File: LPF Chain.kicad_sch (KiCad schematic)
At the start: 24 parts

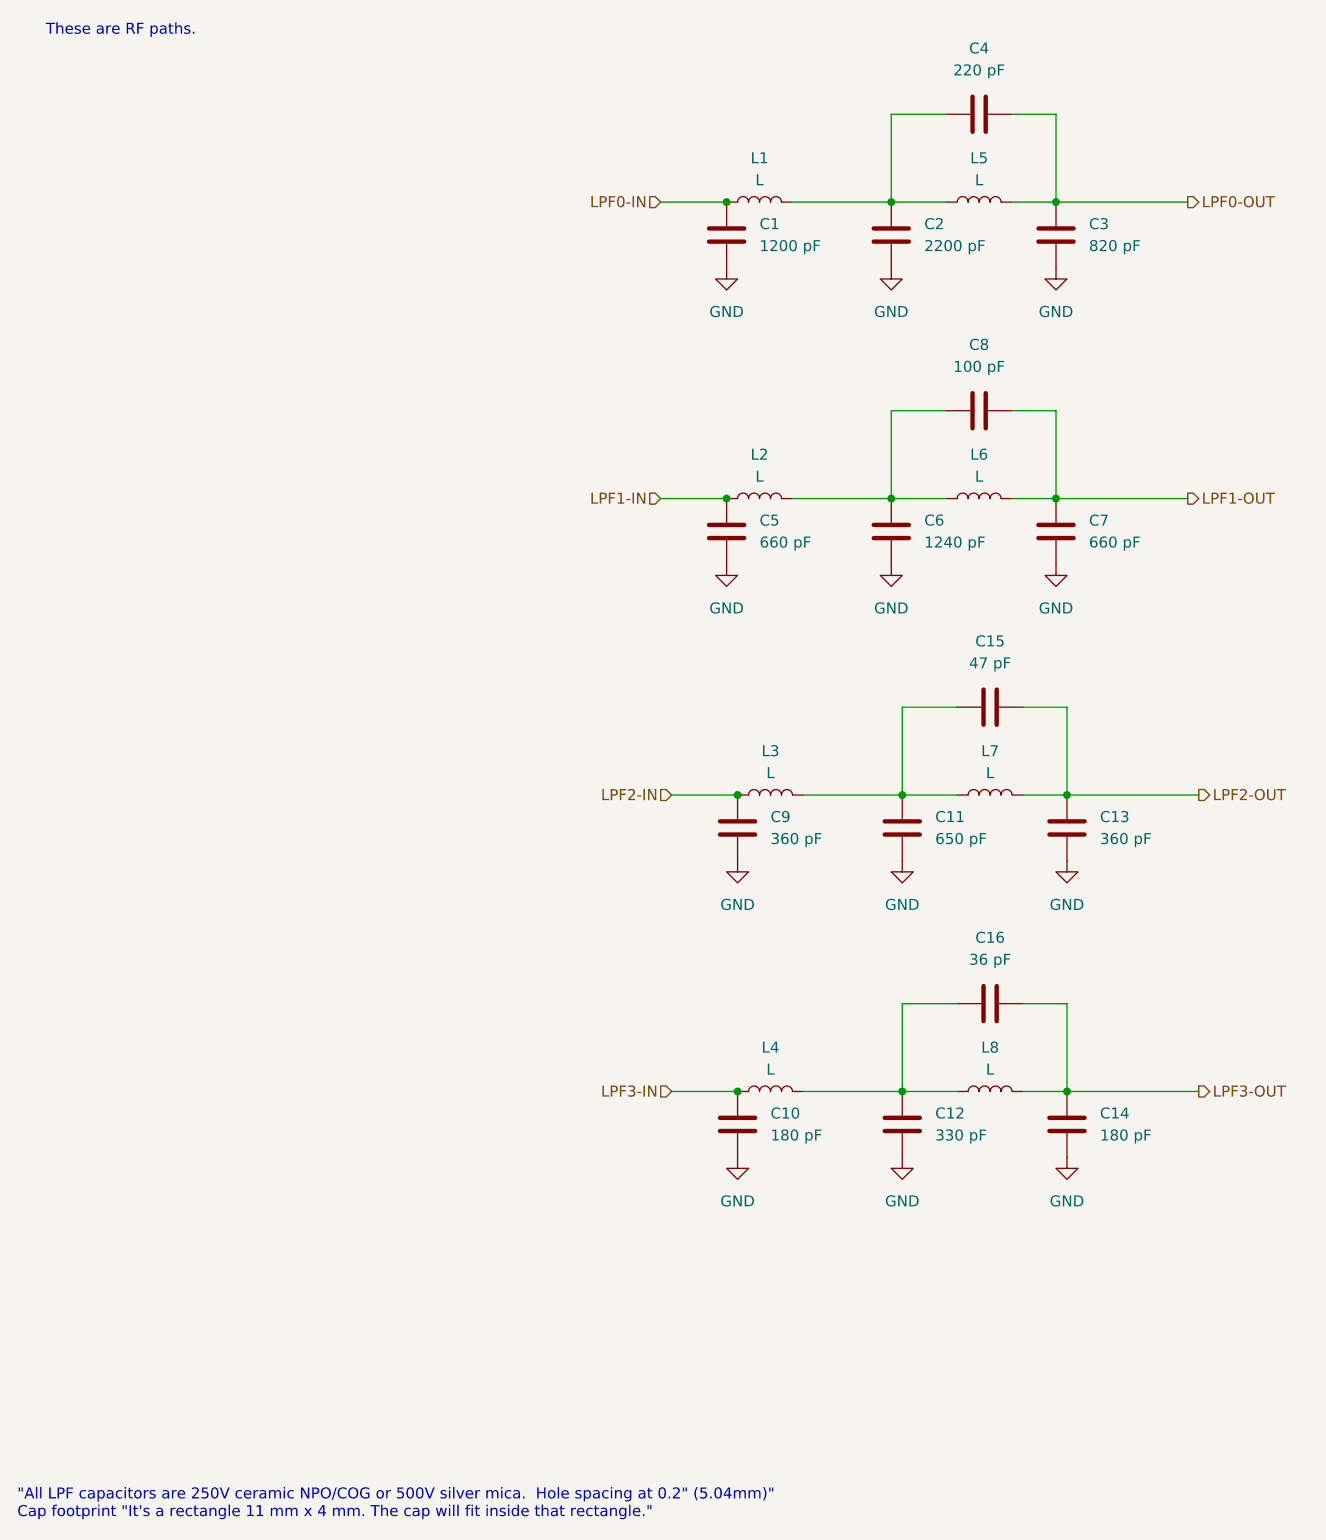
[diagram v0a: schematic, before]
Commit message: expended to all 6 LPFs.  ERC pass.  Need to check component values on new LPF page
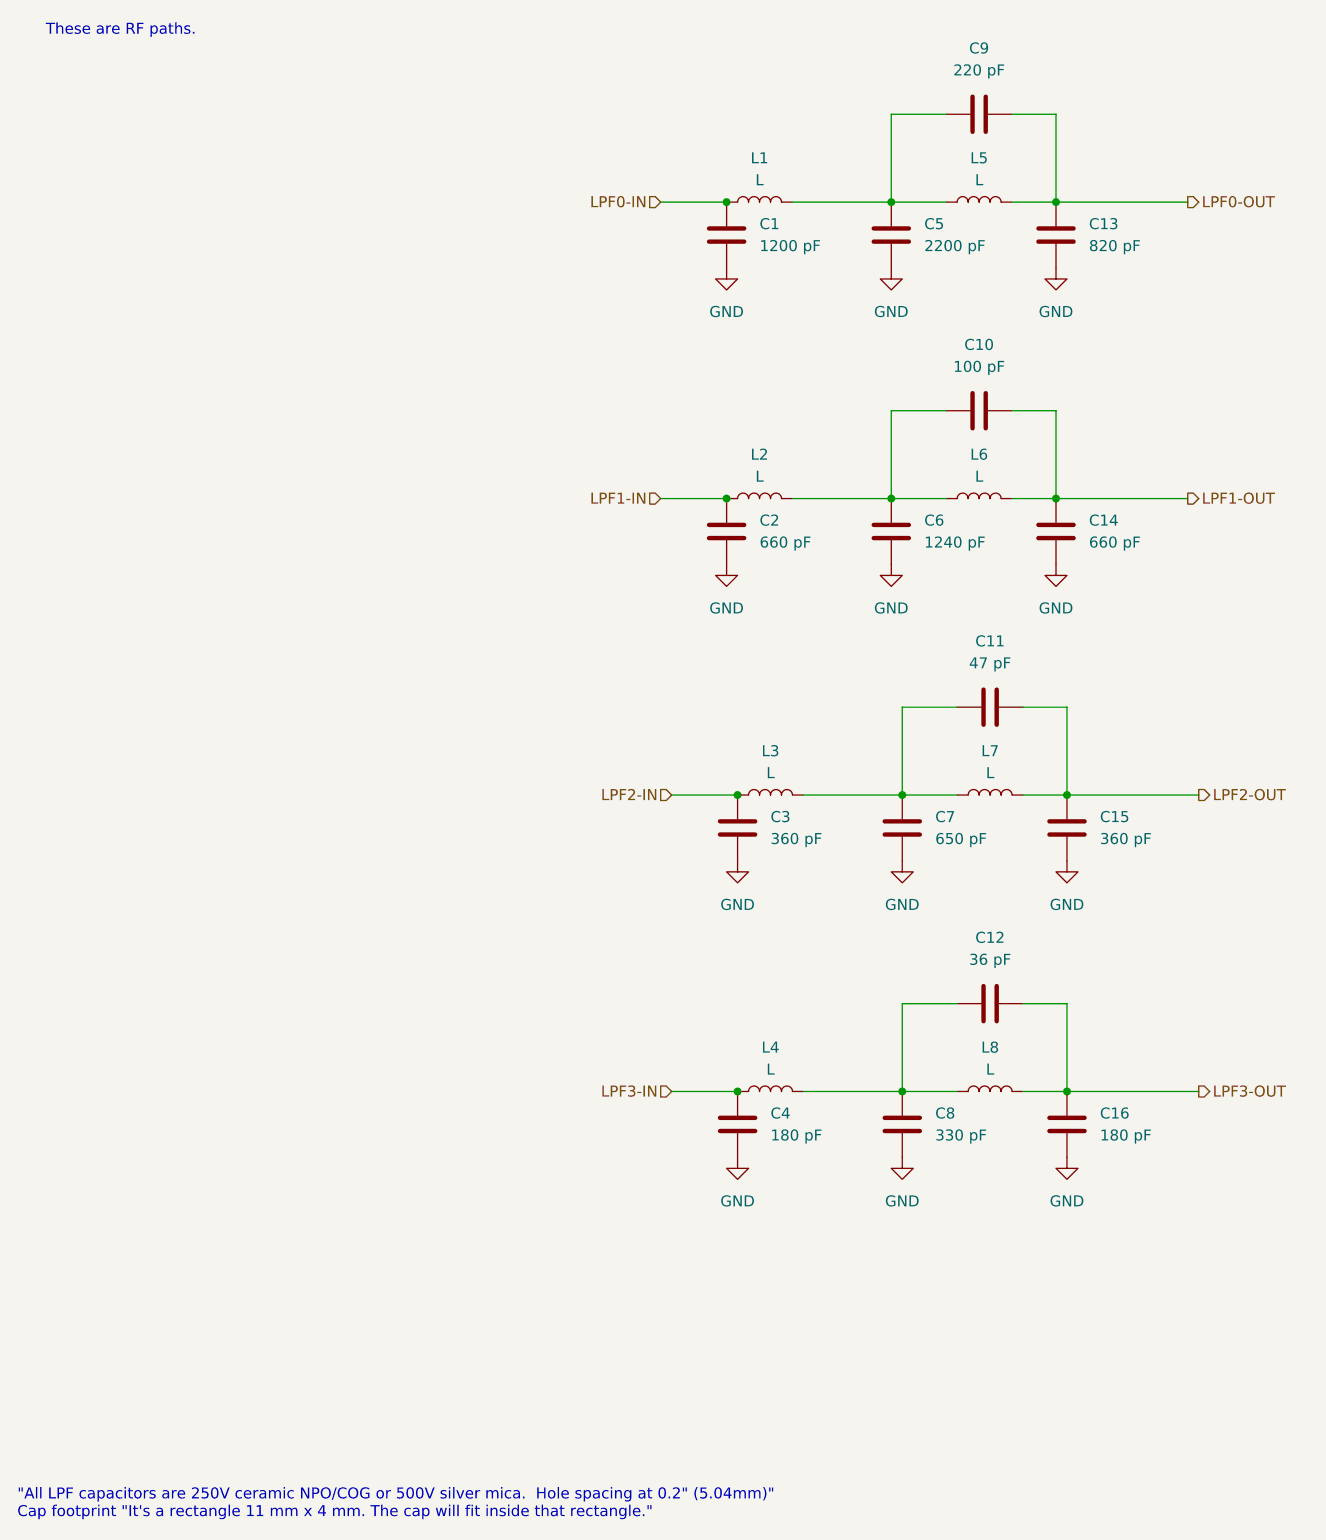
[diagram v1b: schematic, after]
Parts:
- renumbered C8 to C10, C15 to C11, C16 to C12, C3 to C13, C7 to C14, C13 to C15, C14 to C16, C5 to C2, C9 to C3, C10 to C4, C2 to C5, C11 to C7, C12 to C8, C4 to C9

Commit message: v0.10 after slimming down capacitor width to 3mm so it *barely* fits.
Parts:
- C1, C10, C11, C12, C13, C14, C15, C16, C2, C3, C4, C5, C6, C7, C8, C9: footprint ZZZMyLibrary:C_Disc_D11.0mm_W4.0mm_P5.00mm -> ZZZMyLibrary:C_Disc_D11.0mm_W3.0mm_P5.00mm
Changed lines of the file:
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@@
 			)
 		)
-		(property "Footprint" "ZZZMyLibrary:C_Disc_D11.0mm_W4.0mm_P5.00mm"
+		(property "Footprint" "ZZZMyLibrary:C_Disc_D11.0mm_W3.0mm_P5.00mm"
 			(at 101.2952 49.53 0)
 			(effects
@@
 			)
 		)
-		(property "Footprint" "ZZZMyLibrary:C_Disc_D11.0mm_W4.0mm_P5.00mm"
+		(property "Footprint" "ZZZMyLibrary:C_Disc_D11.0mm_W3.0mm_P5.00mm"
 			(at 133.35 30.7848 0)
 			(effects
@@
 			)
 		)
-		(property "Footprint" "ZZZMyLibrary:C_Disc_D11.0mm_W4.0mm_P5.00mm"
+		(property "Footprint" "ZZZMyLibrary:C_Disc_D11.0mm_W3.0mm_P5.00mm"
 			(at 139.3952 49.53 0)
 			(effects
@@
 			)
 		)
-		(property "Footprint" "ZZZMyLibrary:C_Disc_D11.0mm_W4.0mm_P5.00mm"
+		(property "Footprint" "ZZZMyLibrary:C_Disc_D11.0mm_W3.0mm_P5.00mm"
 			(at 121.6152 152.4 0)
 			(effects
@@
 			)
 		)
-		(property "Footprint" "ZZZMyLibrary:C_Disc_D11.0mm_W4.0mm_P5.00mm"
+		(property "Footprint" "ZZZMyLibrary:C_Disc_D11.0mm_W3.0mm_P5.00mm"
 			(at 102.5652 152.4 0)
 			(effects
@@
 			)
 		)
-		(property "Footprint" "ZZZMyLibrary:C_Disc_D11.0mm_W4.0mm_P5.00mm"
+		(property "Footprint" "ZZZMyLibrary:C_Disc_D11.0mm_W3.0mm_P5.00mm"
 			(at 133.35 65.0748 0)
 			(effects
@@
 			)
 		)
-		(property "Footprint" "ZZZMyLibrary:C_Disc_D11.0mm_W4.0mm_P5.00mm"
+		(property "Footprint" "ZZZMyLibrary:C_Disc_D11.0mm_W3.0mm_P5.00mm"
 			(at 121.6152 118.11 0)
 			(effects
@@
 			)
 		)
-		(property "Footprint" "ZZZMyLibrary:C_Disc_D11.0mm_W4.0mm_P5.00mm"
+		(property "Footprint" "ZZZMyLibrary:C_Disc_D11.0mm_W3.0mm_P5.00mm"
 			(at 134.62 99.3648 0)
 			(effects
@@
 			)
 		)
-		(property "Footprint" "ZZZMyLibrary:C_Disc_D11.0mm_W4.0mm_P5.00mm"
+		(property "Footprint" "ZZZMyLibrary:C_Disc_D11.0mm_W3.0mm_P5.00mm"
 			(at 118.4148 41.91 0)
 			(effects
@@
 			)
 		)
-		(property "Footprint" "ZZZMyLibrary:C_Disc_D11.0mm_W4.0mm_P5.00mm"
+		(property "Footprint" "ZZZMyLibrary:C_Disc_D11.0mm_W3.0mm_P5.00mm"
 			(at 102.5652 118.11 0)
 			(effects
@@
 			)
 		)
-		(property "Footprint" "ZZZMyLibrary:C_Disc_D11.0mm_W4.0mm_P5.00mm"
+		(property "Footprint" "ZZZMyLibrary:C_Disc_D11.0mm_W3.0mm_P5.00mm"
 			(at 140.6652 152.4 0)
 			(effects
@@
 			)
 		)
-		(property "Footprint" "ZZZMyLibrary:C_Disc_D11.0mm_W4.0mm_P5.00mm"
+		(property "Footprint" "ZZZMyLibrary:C_Disc_D11.0mm_W3.0mm_P5.00mm"
 			(at 101.2952 83.82 0)
 			(effects
@@
 			)
 		)
-		(property "Footprint" "ZZZMyLibrary:C_Disc_D11.0mm_W4.0mm_P5.00mm"
+		(property "Footprint" "ZZZMyLibrary:C_Disc_D11.0mm_W3.0mm_P5.00mm"
 			(at 139.3952 83.82 0)
 			(effects
@@
 			)
 		)
-		(property "Footprint" "ZZZMyLibrary:C_Disc_D11.0mm_W4.0mm_P5.00mm"
+		(property "Footprint" "ZZZMyLibrary:C_Disc_D11.0mm_W3.0mm_P5.00mm"
 			(at 134.62 133.6548 0)
 			(effects
@@
 			)
 		)
-		(property "Footprint" "ZZZMyLibrary:C_Disc_D11.0mm_W4.0mm_P5.00mm"
+		(property "Footprint" "ZZZMyLibrary:C_Disc_D11.0mm_W3.0mm_P5.00mm"
 			(at 120.3452 83.82 0)
 			(effects
@@
 			)
 		)
-		(property "Footprint" "ZZZMyLibrary:C_Disc_D11.0mm_W4.0mm_P5.00mm"
+		(property "Footprint" "ZZZMyLibrary:C_Disc_D11.0mm_W3.0mm_P5.00mm"
 			(at 140.6652 118.11 0)
 			(effects
